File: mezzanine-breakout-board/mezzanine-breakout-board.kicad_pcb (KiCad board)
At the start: 2 copper layers, 29 x 30 mm, 2 parts, among them J1 Mezzanine Plug, J2 Conn_01x10

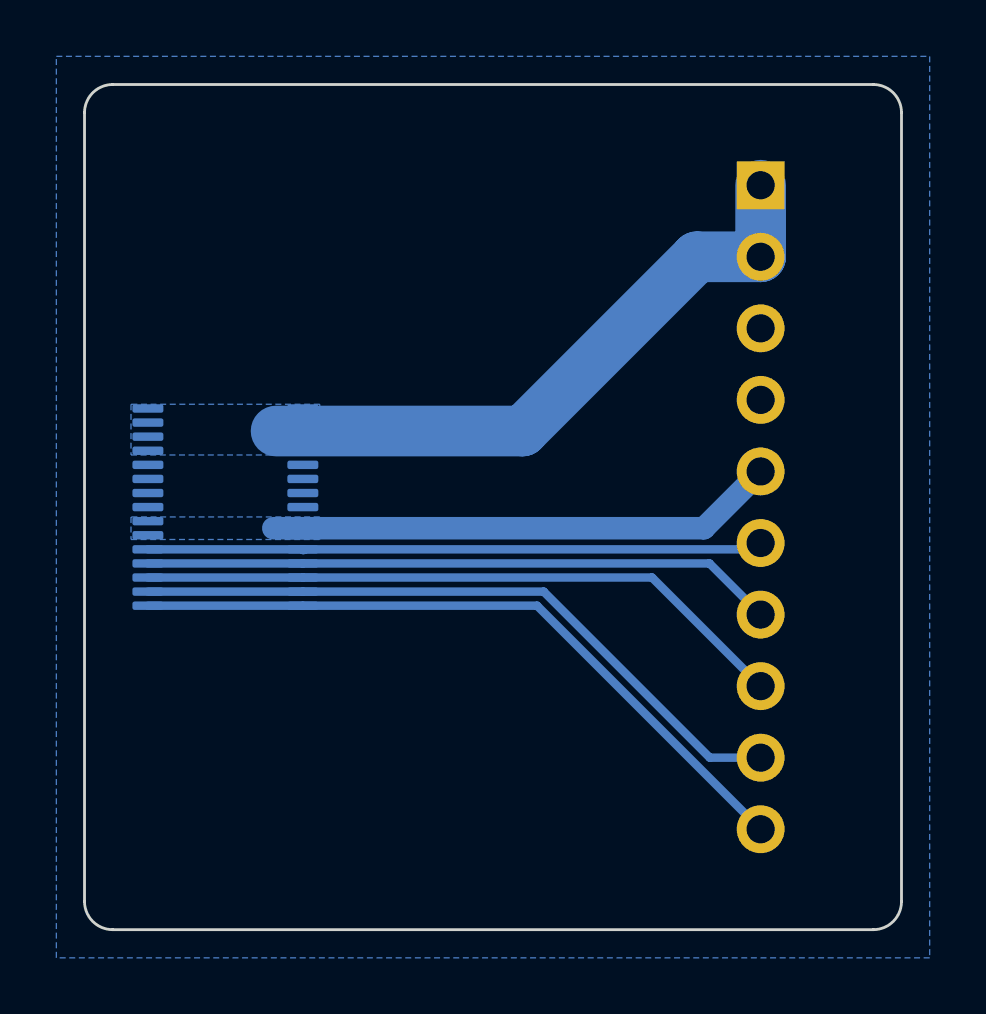
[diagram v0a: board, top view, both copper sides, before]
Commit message: Updated RW mezzanine breakout to be 2 sided osh park PCB with silk and everything. Made shorter to try and fit with ADCS card below the RW board, and avoid RW board fasteners.
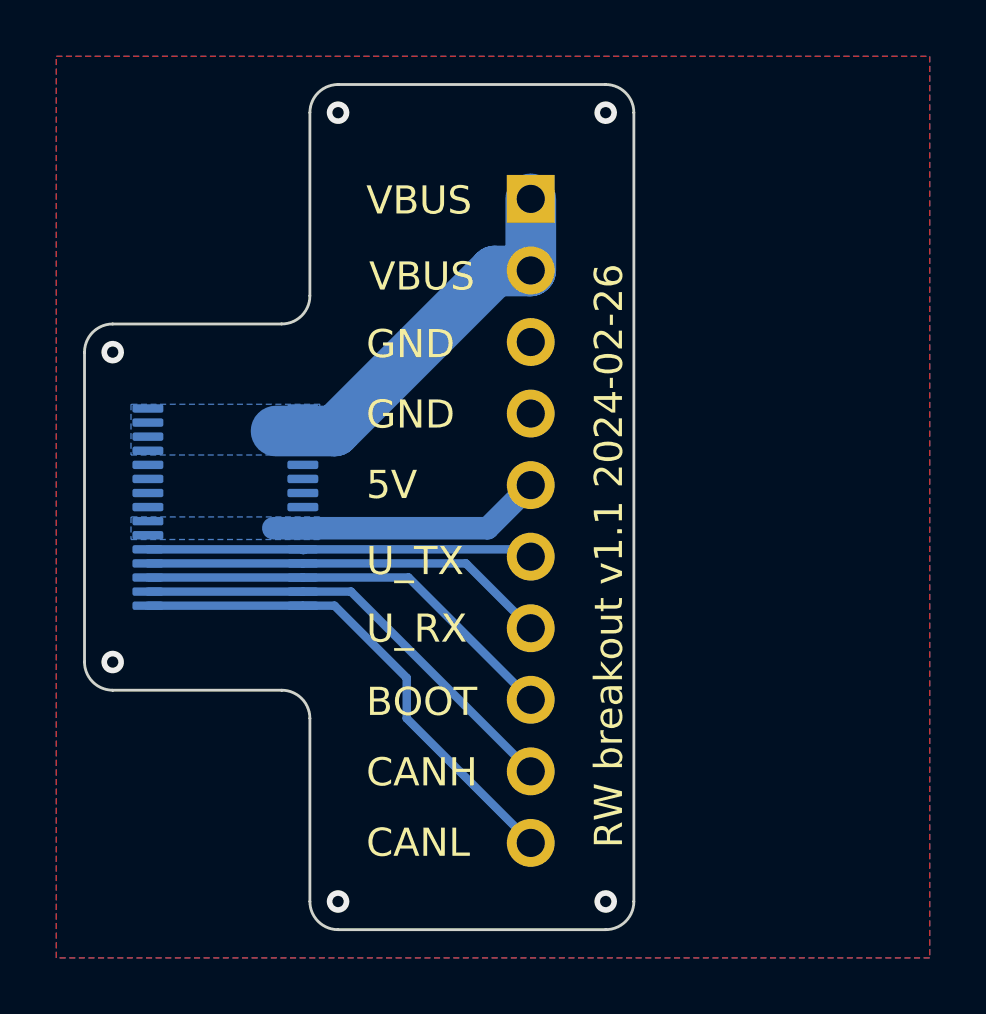
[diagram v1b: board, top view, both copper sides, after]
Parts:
- moved J2 8.17 mm to (132.8, 95.1)
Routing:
- net /VBUS: track 22.3 -> 13.9 mm
- net /5V: track 18.1 -> 9.77 mm
- net /UART_TX: track 21.9 -> 13.8 mm
- net /CAN_H: track 24.2 -> 16.2 mm
- net /UART_RX: track 22.5 -> 14.5 mm
- net /BOOT: track 23.3 -> 15.4 mm
- net /CAN_L: track 25.0 -> 17.9 mm
- net /GND: vias 0 -> 6
- added copper zone on F.Cu, net /GND
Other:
- board size 29 x 30 mm -> 19.5 x 30 mm
- board text added: "5V"
- board text added: "BOOT"
- board text added: "CANH"
- board text added: "CANL"
- board text added: "GND"
- board text added: "RW breakout v1.1 2024-02-26"
- board text added: "U_RX"
- board text added: "U_TX"
- board text added: "VBUS"

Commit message: version, date, and possibly other changes and switched to v8
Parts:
- J2: footprint Connector_PinHeader_2.54mm:PinHeader_1x10_P2.54mm_Vertical -> Connector_PinHeader_2.54mm:PinHeader_1x08_P2.54mm_Vertical; moved to F.Cu
- moved J2 5.26 mm to (128.0, 97.1), turned to 0 degrees
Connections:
- J2 pad 2: /VBUS -> /GND
- J2 pad 3: /GND -> /5V
- J2 pad 4: /GND -> /UART_TX
- J2 pad 5: /5V -> /UART_RX
- J2 pad 6: /UART_TX -> /BOOT
- J2 pad 7: /UART_RX -> /CAN_H
- J2 pad 8: /BOOT -> /CAN_L
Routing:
- net /CAN_H: track 16.2 -> 10.7 mm
- net /VBUS: track 13.9 -> 8.42 mm
- net /UART_RX: track 14.5 -> 9.05 mm
- net /BOOT: track 15.4 -> 9.97 mm
- net /CAN_L: track 17.9 -> 12.6 mm
- net /UART_TX: track 13.8 -> 9.59 mm
- net /5V: track 9.77 -> 6.52 mm
- net /GND: vias 6 -> 5
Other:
- board size 19.5 x 30 mm -> 12.2 x 21.2 mm
- board text added: "C_H"
- board text added: "C_L"
- board text added: "RW breakout v1.2 2024-03-12"
- board text removed: "CANH"
- board text removed: "CANL"
- board text removed: "RW breakout v1.1 2024-02-26"
